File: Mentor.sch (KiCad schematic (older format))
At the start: 41 parts, among them J1 CONN_01X02, J2 CONN_01X06, J3 CONN_01X09, J4 CONN_01X10, J5 CONN_01X02, J6 CONN_01X03, J7 CONN_01X09, Q1 PZT2222A, Q2 PZT2222A, Q3 IRFR3303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

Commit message: RTM2, via, prototype picture, gerber added
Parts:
- R4: value R -> 330
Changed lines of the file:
@@
 P 6300 2950
 F 0 "R4" V 6380 2950 50  0000 C CNN
-F 1 "R" V 6300 2950 50  0000 C CNN
+F 1 "330" V 6300 2950 50  0000 C CNN
 F 2 "Resistors_SMD:R_0805_HandSoldering" V 6230 2950 50  0001 C CNN
 F 3 "" H 6300 2950 50  0001 C CNN

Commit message: buzzer changed
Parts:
- BZ1: footprint Buzzers_Beepers:MagneticBuzzer_Kingstate_KCG0601 -> Buzzers_Beepers:Buzzer_12x9.5RM7.6
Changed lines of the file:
@@
 F 0 "BZ1" V 7450 4400 50  0000 L CNN
 F 1 "Buzzer" V 7350 4300 50  0000 L CNN
-F 2 "Buzzers_Beepers:MagneticBuzzer_Kingstate_KCG0601" V 7175 4500 50  0001 C CNN
+F 2 "Buzzers_Beepers:Buzzer_12x9.5RM7.6" V 7175 4500 50  0001 C CNN
 F 3 "" V 7175 4500 50  0001 C CNN
 	1    7200 4400

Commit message: minor changes, Gerber and BOM added
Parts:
- C6: value C -> 100n
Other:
- moved on the sheet: J1
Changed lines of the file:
@@
 P 7600 3750
 F 0 "C6" H 7625 3850 50  0000 L CNN
-F 1 "C" H 7625 3650 50  0000 L CNN
+F 1 "100n" H 7625 3650 50  0000 L CNN
 F 2 "Capacitors_SMD:C_0805_HandSoldering" H 7638 3600 50  0001 C CNN
 F 3 "" H 7600 3750 50  0001 C CNN
@@
 Wire Wire Line
 	2750 1600 2750 1650
-Wire Wire Line
-	1300 1400 1950 1400
 Connection ~ 1700 1400
 Connection ~ 1850 1400
@@
 L +12V #PWR039
 U 1 1 59267090
-P 1500 1400
-F 0 "#PWR039" H 1500 1250 50  0001 C CNN
-F 1 "+12V" H 1500 1540 50  0000 C CNN
-F 2 "" H 1500 1400 50  0001 C CNN
-F 3 "" H 1500 1400 50  0001 C CNN
-	1    1500 1400
+P 1150 1400
+F 0 "#PWR039" H 1150 1250 50  0001 C CNN
+F 1 "+12V" H 1150 1540 50  0000 C CNN
+F 2 "" H 1150 1400 50  0001 C CNN
+F 3 "" H 1150 1400 50  0001 C CNN
+	1    1150 1400
 	1    0    0    -1
 $EndComp
@@
 L CONN_01X02 J1
 U 1 1 59267126
-P 1100 1450
-F 0 "J1" H 1100 1600 50  0000 C CNN
-F 1 "CONN_01X02" V 1200 1450 50  0000 C CNN
-F 2 "conn_kk100:kk100_22-23-2021" H 1100 1450 50  0001 C CNN
-F 3 "" H 1100 1450 50  0001 C CNN
-	1    1100 1450
+P 900 1450
+F 0 "J1" H 900 1600 50  0000 C CNN
+F 1 "CONN_01X02" V 1000 1450 50  0000 C CNN
+F 2 "conn_kk100:kk100_22-23-2021" H 900 1450 50  0001 C CNN
+F 3 "" H 900 1450 50  0001 C CNN
+	1    900  1450
 	-1   0    0    -1
 $EndComp
@@
 L GND #PWR040
 U 1 1 592672F6
-P 1300 1600
-F 0 "#PWR040" H 1300 1350 50  0001 C CNN
-F 1 "GND" H 1300 1450 50  0000 C CNN
-F 2 "" H 1300 1600 50  0001 C CNN
-F 3 "" H 1300 1600 50  0001 C CNN
-	1    1300 1600
-	1    0    0    -1
-$EndComp
-Wire Wire Line
-	1300 1500 1300 1600
+P 1100 1600
+F 0 "#PWR040" H 1100 1350 50  0001 C CNN
+F 1 "GND" H 1100 1450 50  0000 C CNN
+F 2 "" H 1100 1600 50  0001 C CNN
+F 3 "" H 1100 1600 50  0001 C CNN
+	1    1100 1600
+	1    0    0    -1
+$EndComp
+Wire Wire Line
+	1100 1500 1100 1600
 Connection ~ 1550 1400
-Connection ~ 1500 1400
 Text Notes 4400 1300 2    39   ~ 0
 From Amp
@@
 	1    0    0    -1
 $EndComp
+Wire Wire Line
+	1100 1400 1950 1400
+Connection ~ 1150 1400
 $EndSCHEMATC

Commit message: Mentor V2 RTM
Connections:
- net LCD03: now also U2.26 (D8); no longer U2.27 (#D9)
- net LCD04: now also U2.27 (#D9); no longer U2.26 (D8)
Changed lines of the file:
@@
 EESchema Schematic File Version 2
-LIBS:power
-LIBS:device
-LIBS:transistors
-LIBS:conn
-LIBS:regul
-LIBS:display
 LIBS:arduino_nano
 LIBS:ee2-5nu
 LIBS:l_cap
-LIBS:7805d-pack
+LIBS:Connector_Generic
+LIBS:Diode
+LIBS:Display_Character
+LIBS:LED
+LIBS:power
+LIBS:Regulator_Linear
+LIBS:Relay
 LIBS:Mentor-cache
 EELAYER 25 0
@@
 Text GLabel 6300 4050 2    39   Input ~ 0
 LCD02
-Text GLabel 6300 3950 2    39   Input ~ 0
+Text GLabel 6300 3850 2    39   Input ~ 0
 LCD04
 Text GLabel 6300 3550 2    39   Input ~ 0
@@
 Text GLabel 6300 3750 2    39   Input ~ 0
 LCDE2
-Text GLabel 6300 3850 2    39   Input ~ 0
+Text GLabel 6300 3950 2    39   Input ~ 0
 LCD03
 Text GLabel 8900 3650 0    39   Input ~ 0
@@
 Text Notes 8100 7650 0    60   ~ 0
 May24th 2017
-Text Notes 9500 3250 1    60   ~ 0
+Text Notes 9600 3500 1    60   ~ 0
 4x40 Display
 $Comp
@@
 U 1 1 59283D43
 P 9150 3250
-F 0 "J7" H 9500 3100 50  0000 C CNN
-F 1 "CONN_01X09" V 9250 3250 50  0000 C CNN
+F 0 "J7" V 9350 3600 50  0000 C CNN
+F 1 "CONN_01X09" V 9350 3300 50  0000 C CNN
 F 2 "conn_kk100:kk100_22-23-2091" H 9150 3250 50  0001 C CNN
 F 3 "" H 9150 3250 50  0001 C CNN

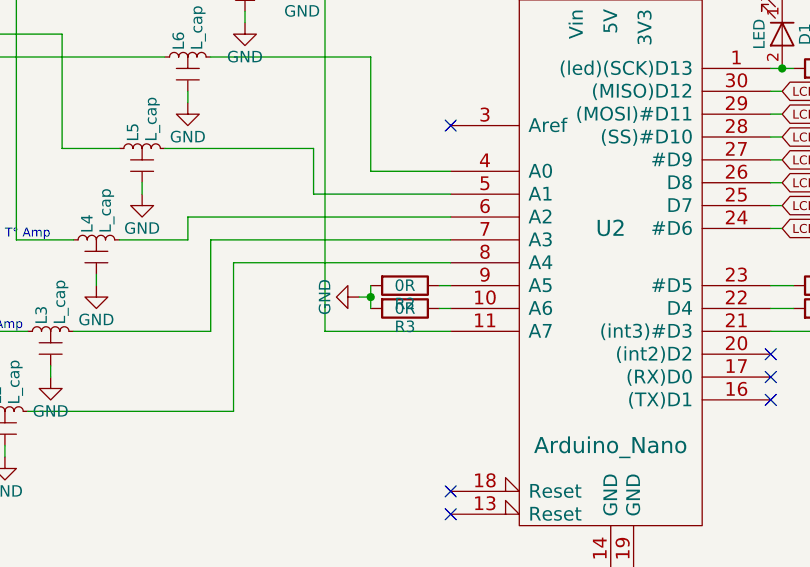
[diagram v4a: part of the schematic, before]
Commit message: minor routing fix, V2 ok
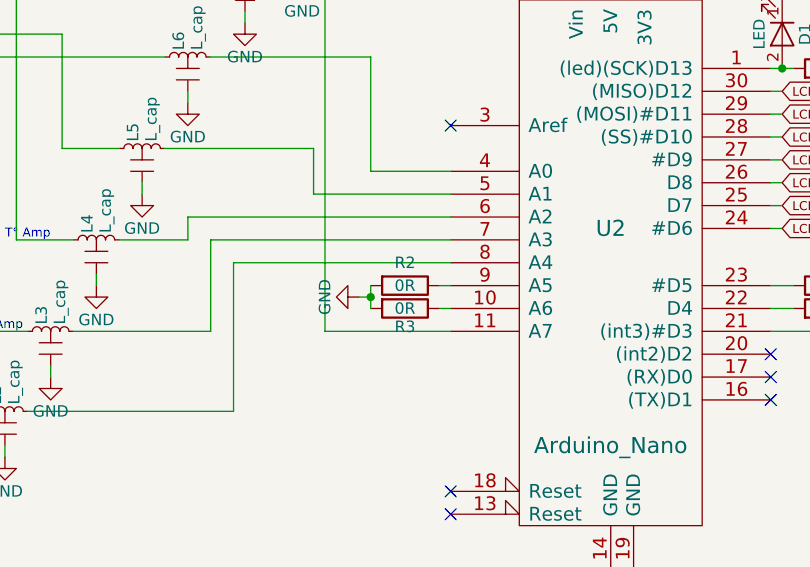
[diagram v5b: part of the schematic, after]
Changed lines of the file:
@@
 U 1 1 592521F1
 P 4650 4400
-F 0 "R2" V 4730 4400 50  0000 C CNN
+F 0 "R2" V 4550 4400 50  0000 C CNN
 F 1 "0R" V 4650 4400 50  0000 C CNN
 F 2 "Resistors_SMD:R_0805_HandSoldering" V 4580 4400 50  0001 C CNN

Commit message: upgrade to kicad 5.x
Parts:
- BZ1: symbol Buzzer -> Mentor-rescue:Buzzer
- C1, C3, C5: symbol C_Small -> Mentor-rescue:C_Small
- C2, C4: symbol CP1_Small -> Mentor-rescue:CP1_Small
- C6: symbol C -> Mentor-rescue:C
- D1: symbol LED -> Mentor-rescue:LED
- J1, J5: symbol CONN_01X02 -> Mentor-rescue:CONN_01X02
- J2: symbol CONN_01X06 -> Mentor-rescue:CONN_01X06
- J3, J7: symbol CONN_01X09 -> Mentor-rescue:CONN_01X09
- J4: symbol CONN_01X10 -> Mentor-rescue:CONN_01X10
- J6: symbol CONN_01X03 -> Mentor-rescue:CONN_01X03
- L1, L2, L3, L4, L5, L6: symbol L_cap -> l_cap:L_cap
- Q1, Q2: symbol PZT2222A -> Mentor-rescue:PZT2222A
- Q3: symbol IRF3205 -> Mentor-rescue:IRF3205
- R1, R2, R3, R4, R5, R6, R7, R8, R9: symbol R -> Mentor-rescue:R
- RL1: symbol EC2-5NU -> ee2-5nu:EC2-5NU
- RV1: symbol POT -> Mentor-rescue:POT
- TP1, TP2, TP3, TP4: symbol TEST -> Mentor-rescue:TEST
- U1: symbol KA78M05_TO252 -> Mentor-rescue:KA78M05_TO252
- U2: symbol Arduino_Nano -> arduino_nano:Arduino_Nano

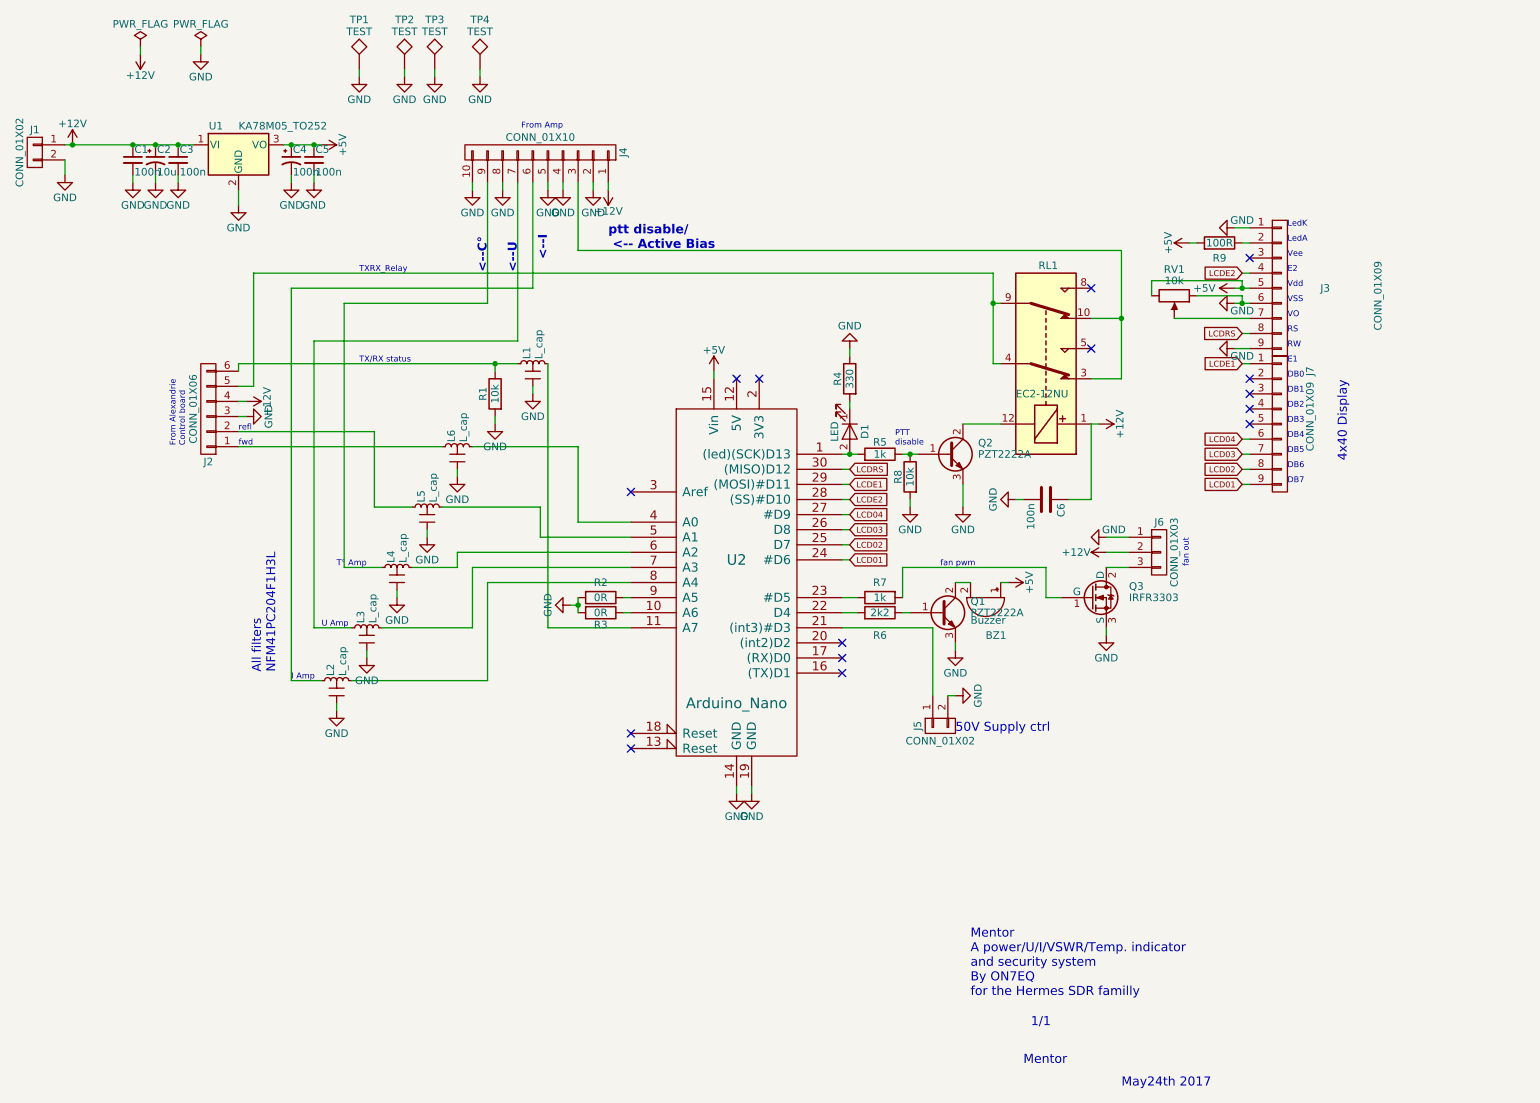
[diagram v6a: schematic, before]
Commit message: full W6PQL compatible version
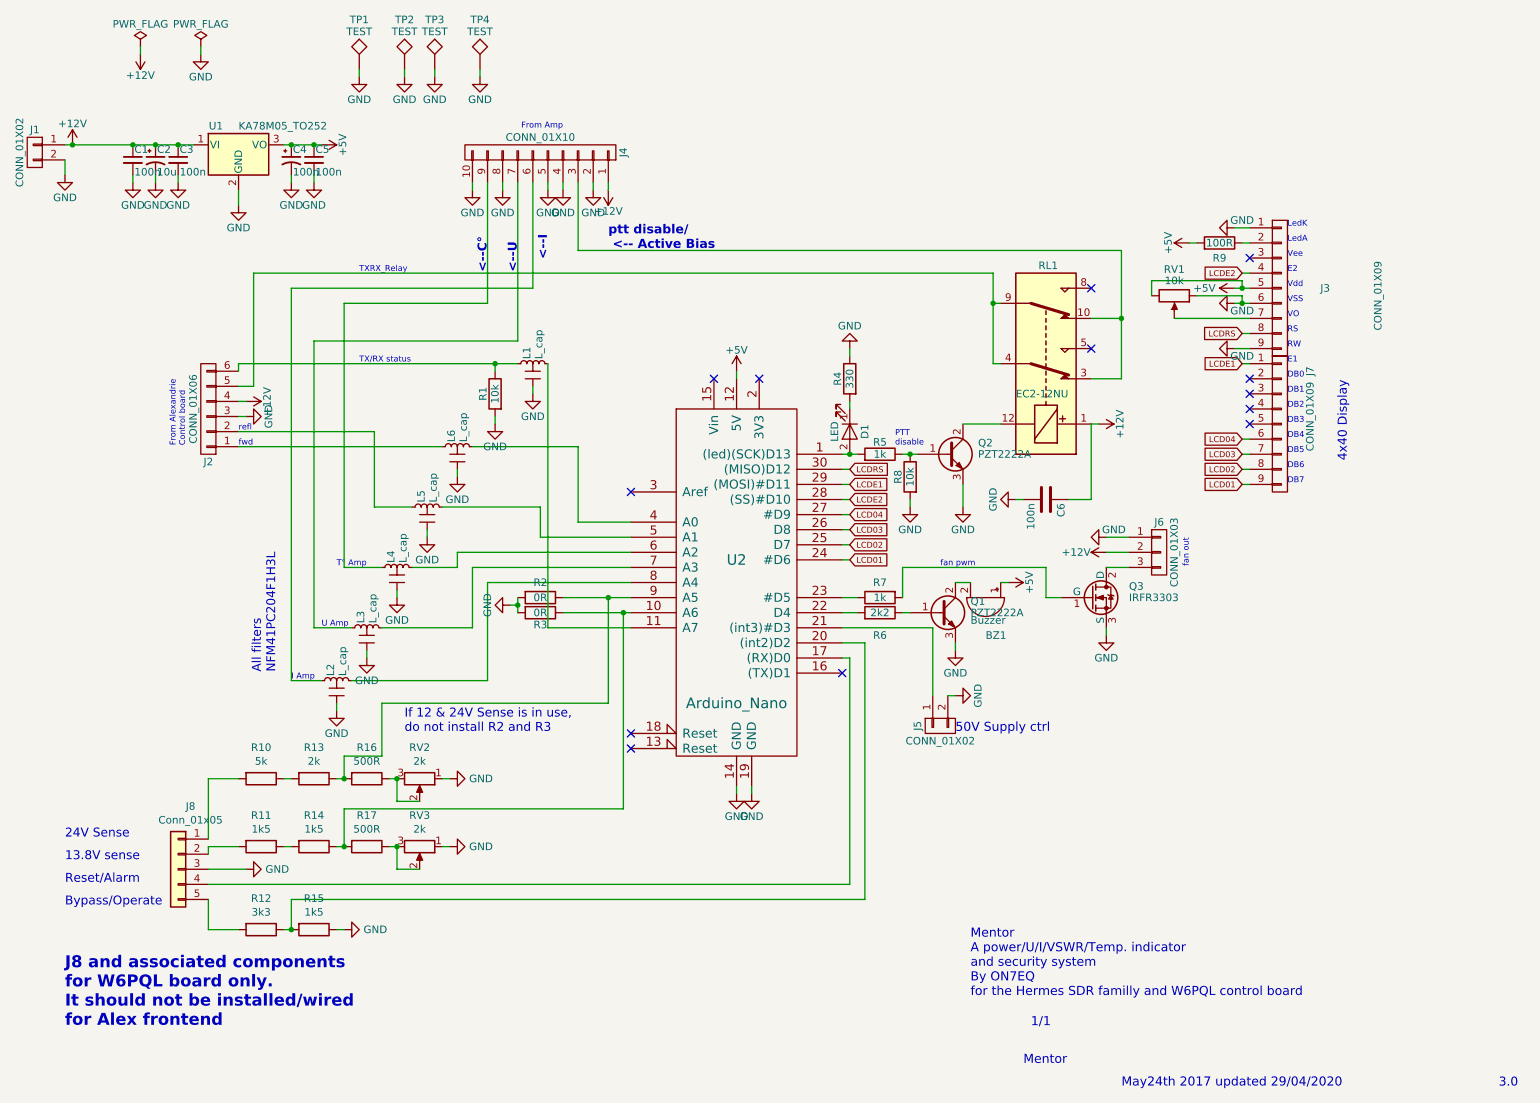
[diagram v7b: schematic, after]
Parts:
- added J8: Conn_01x05, conn_kk100:kk100_22-23-2051, symbol Connector_Generic:Conn_01x05
- added R10: 5k, Resistor_SMD:R_0805_2012Metric_Pad1.15x1.40mm_HandSolder, symbol Device:R
- added R11, R14, R15: 1k5, Resistor_SMD:R_0805_2012Metric_Pad1.15x1.40mm_HandSolder, symbol Device:R
- added R12: 3k3, Resistor_SMD:R_0805_2012Metric_Pad1.15x1.40mm_HandSolder, symbol Device:R
- added R13: 2k, Resistor_SMD:R_0805_2012Metric_Pad1.15x1.40mm_HandSolder, symbol Device:R
- added R16, R17: 500R, Resistor_SMD:R_0805_2012Metric_Pad1.15x1.40mm_HandSolder, symbol Device:R
- added RV2, RV3: 2k, Trimmer_3314G1_Handsoldering:Trimmer_3314G1_Handsoldering, symbol Device:R_POT
- BZ1: footprint Buzzers_Beepers:Buzzer_12x9.5RM7.6 -> Buzzer_Beeper:Buzzer_12x9.5RM7.6
- C1, C3, C4, C5, C6: footprint Capacitors_SMD:C_0805_HandSoldering -> Capacitor_SMD:C_0805_2012Metric_Pad1.15x1.40mm_HandSolder
- C2: footprint Capacitors_Tantalum_SMD:CP_Tantalum_Case-C_EIA-6032-28_Hand -> Capacitor_Tantalum_SMD:CP_EIA-6032-28_Kemet-C_Pad2.25x2.35mm_HandSolder
- D1: footprint Diodes_SMD:D_0805 -> Diode_SMD:D_0805_2012Metric_Pad1.15x1.40mm_HandSolder
- Q1, Q2: footprint TO_SOT_Packages_SMD:SOT-223 -> Package_TO_SOT_SMD:SOT-223
- Q3, U1: footprint TO_SOT_Packages_SMD:TO-252-3_TabPin2 -> Package_TO_SOT_SMD:TO-252-3_TabPin2
- R1, R2, R3, R4, R5, R6, R7, R8, R9: footprint Resistors_SMD:R_0805_HandSoldering -> Resistor_SMD:R_0805_2012Metric_Pad1.15x1.40mm_HandSolder
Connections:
- net +5V: now also U2.12 (5V); no longer U2.15 (Vin)
- net GND: now also J8.3 (Pin_3), R15.1, RV2.1, RV3.1
- net at R3.1, U2.10 (A6): now also R14.1, R17.2
- net at U2.17 ((RX)D0): now also J8.4 (Pin_4)
- net at U2.20 ((int2)D2): now also R12.1, R15.2
- net at R2.1, U2.9 (A5): now also R13.1, R16.2
- new net: R10.1, R13.2
- new net: J8.1 (Pin_1), R10.2
- new net: R16.1, RV2.2, RV2.3
- new net: J8.2 (Pin_2), R11.2
- new net: J8.5 (Pin_5), R12.2
- new net: R11.1, R14.2
- new net: R17.1, RV3.2, RV3.3
- no-connect marks 15 -> 13
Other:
- note added: "13.8V sense"
- note added: "24V Sense"
- note added: "3.0\n"
- note added: "Bypass/Operate\n"
- note added: "If 12 & 24V Sense is in use, \ndo not install R2 and R3"
- note added: "J8 and associated components \nfor W6PQL board only. \nIt should not be installed/wired\nfor Alex frontend"
- note added: "May24th 2017 updated 29/04/2020\n"
- note added: "Mentor\nA power/U/I/VSWR/Temp. indicator\nand security system\nBy ON7EQ\nfor the Hermes SDR familly and W6PQL control board"
- note added: "Reset/Alarm"
- note removed: "May24th 2017"
- note removed: "Mentor\nA power/U/I/VSWR/Temp. indicator\nand security system\nBy ON7EQ\nfor the Hermes SDR familly"
- moved on the sheet: R2, R3
